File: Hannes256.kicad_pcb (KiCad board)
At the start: 2 copper layers, 56.3 x 82 mm, 33 parts, among them J1 TED_SOCKET, J2 RAM_SELECTOR, J3 CONN_CS, U1 MOS_7360_TED, U10 41256, U11 41256, U12 41256, U13 41256, U14 41256, U2 GAL20V8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

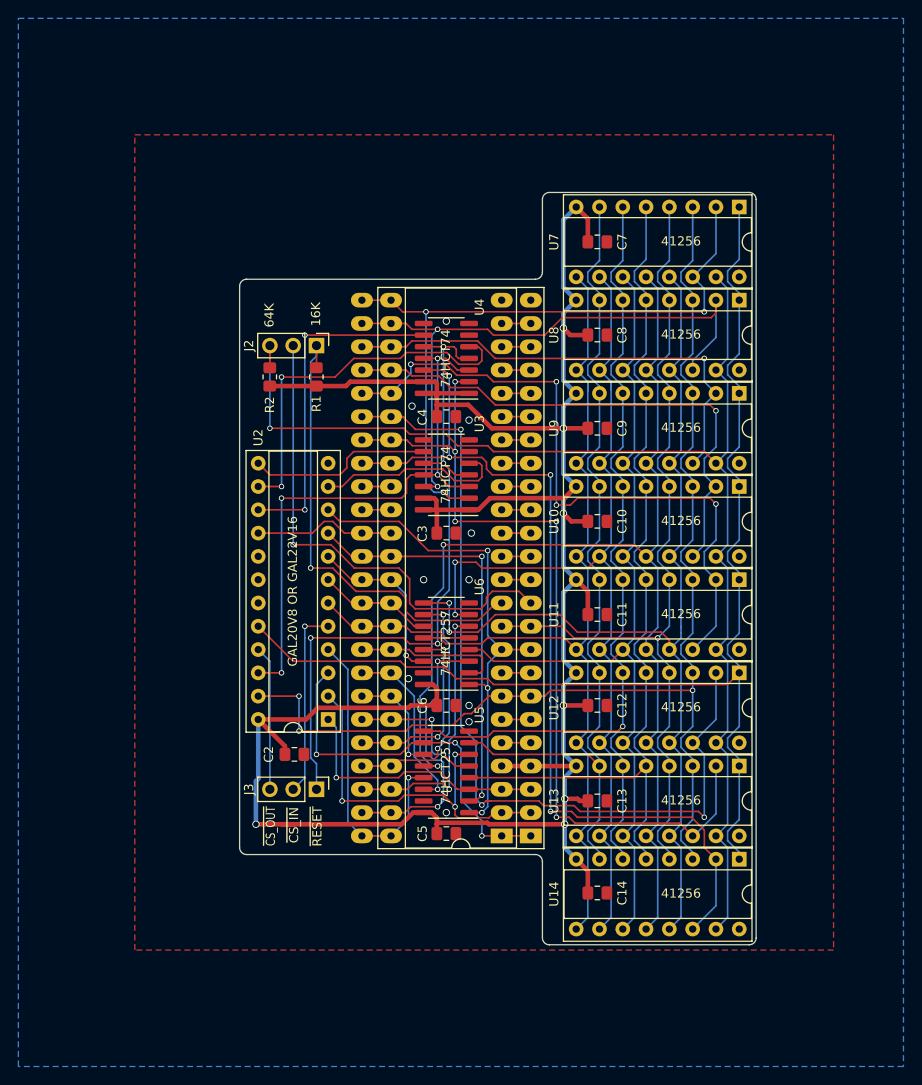
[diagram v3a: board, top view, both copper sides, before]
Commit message: Use a different MOS 6529 replacement circuit, courtesy of TLC
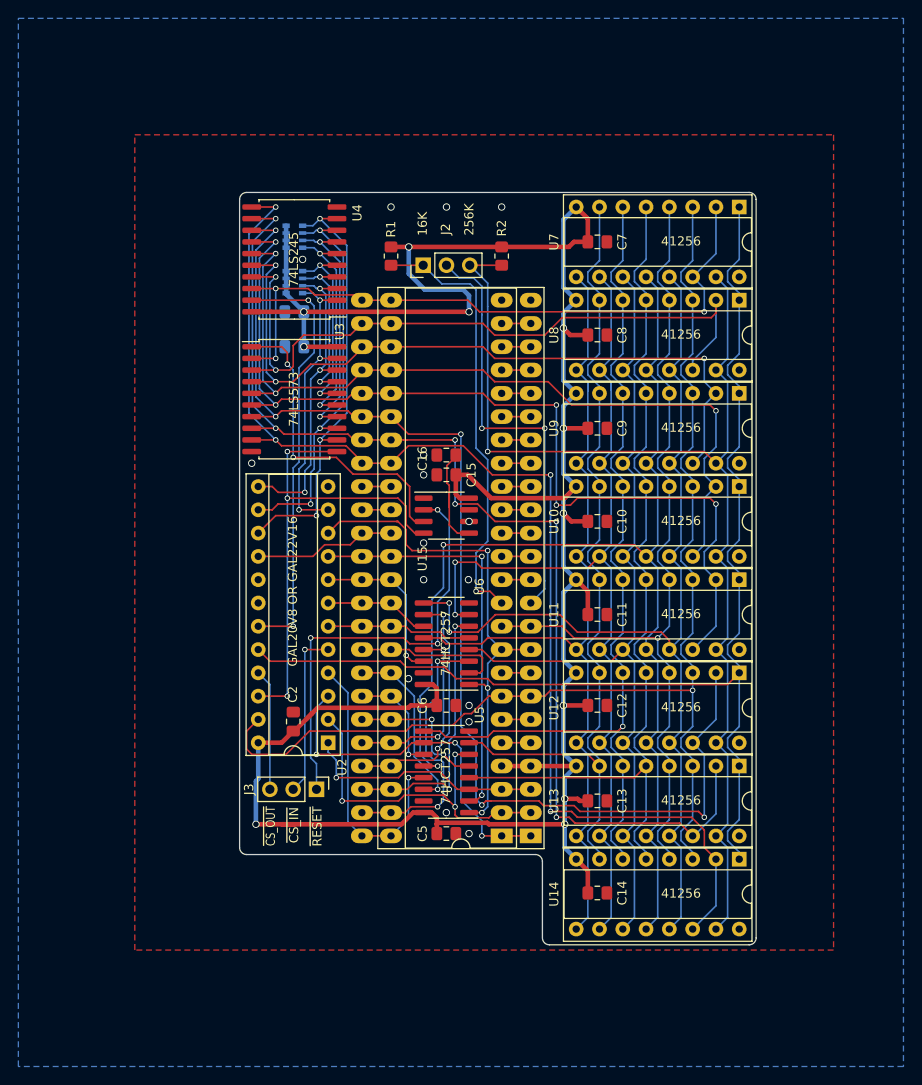
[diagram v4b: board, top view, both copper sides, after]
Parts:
- added C15: 100n, Capacitor_SMD:C_0805_2012Metric_Pad1.18x1.45mm_HandSolder, F.Cu at (126.7, 97.5)
- added C16: 10n, Capacitor_SMD:C_0805_2012Metric_Pad1.18x1.45mm_HandSolder, F.Cu at (126.7, 95.4)
- added RN1: 1k, Resistor_SMD:R_Array_Convex_4x0603, B.Cu at (110.1, 76.5)
- added RN2: 1k, Resistor_SMD:R_Array_Convex_4x0603, B.Cu at (110.1, 71.6)
- added U15: NE555D, Package_SO:SOIC-8_3.9x4.9mm_P1.27mm, F.Cu at (126.7, 102.0)
- C3, C4: moved to B.Cu
- U3: value 74HCT74 -> 74LS573; footprint Package_SO:SOIC-14_3.9x8.7mm_P1.27mm -> Package_SO:SOIC-20W_7.5x12.8mm_P1.27mm
- U4: value 74HCT74 -> 74LS245; footprint Package_SO:SOIC-14_3.9x8.7mm_P1.27mm -> Package_SO:SOIC-20W_7.5x12.8mm_P1.27mm
- moved C3 29.3 mm to (110.1, 79.8), turned to 180 degrees
- moved R2 28.5 mm to (132.7, 73.7), turned to 270 degrees
- moved U4 19.8 mm to (110.1, 74.0)
- moved U3 18.5 mm to (110.1, 89.3), turned to 0 degrees
- moved C4 18.2 mm to (110.1, 83.6), turned to 180 degrees
- moved R1 15.5 mm to (120.7, 73.7), turned to 270 degrees
- moved J2 14.6 mm to (124.2, 74.7), turned to 90 degrees
- moved C2 3.58 mm to (110.0, 124.4), turned to 90 degrees
- moved U2 2.54 mm to (113.8, 126.7)
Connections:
- U2 pad 11: /~RAS~/~CAS~ Generation/p0 -> p0
- U2 pad 13: /~RAS~/~CAS~ Generation/p1 -> p1
- U2 pad 14: /~RAS~/~CAS~ Generation/p6 -> p6
- U2 pad 15: /~RAS~/~CAS~ Generation/p7 -> p7
- U2 pad 19: Net-(U2-Pad19) -> /~RAS~/~CAS~ Generation/~cs_ramrd
- U2 pad 22: /~RAS~/~CAS~ Generation/~cs_ram -> /~RAS~/~CAS~ Generation/~cs_ramwr
- U3 pad 1: +5V -> /~RAS~/~CAS~ Generation/~u3enable
- U3 pad 10: ~RESET -> GND
- U3 pad 11: /~RAS~/~CAS~ Generation/~cs_ram -> /~RAS~/~CAS~ Generation/~cs_ramwr
- U3 pad 12: d1 -> p7
- U3 pad 13: +5V -> p6
- U3 pad 14: +5V -> p5
- U3 pad 3: /~RAS~/~CAS~ Generation/~cs_ram -> d1
- U3 pad 4: ~RESET -> d2
- U3 pad 5: /~RAS~/~CAS~ Generation/p0 -> d3
- U3 pad 6: Net-(U3-Pad6) -> d4
- U3 pad 7: GND -> d5
- U3 pad 8: Net-(U3-Pad8) -> d6
- U3 pad 9: /~RAS~/~CAS~ Generation/p1 -> d7
- U4 pad 10: ~RESET -> GND
- U4 pad 11: /~RAS~/~CAS~ Generation/~cs_ram -> d7
- U4 pad 12: d7 -> d6
- U4 pad 13: +5V -> d5
- U4 pad 14: +5V -> d4
- U4 pad 2: d6 -> p0
- U4 pad 3: /~RAS~/~CAS~ Generation/~cs_ram -> p1
- U4 pad 4: ~RESET -> p2
- U4 pad 5: /~RAS~/~CAS~ Generation/p6 -> p3
- U4 pad 6: Net-(U4-Pad6) -> p4
- U4 pad 7: GND -> p5
- U4 pad 8: Net-(U4-Pad8) -> p6
- U4 pad 9: /~RAS~/~CAS~ Generation/p7 -> p7
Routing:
- net /~RAS~/~CAS~ Generation/~cs_ram: track 62.7 -> 0.00 mm, vias 4 -> 0
- net /~RAS~/~CAS~ Generation/~cs_ramwr: track 0.00 -> 52.9 mm, vias 0 -> 3
- net p7: track 0.00 -> 48.0 mm, vias 0 -> 3
- net /~RAS~/~CAS~ Generation/~cs_ramrd: track 0.00 -> 46.8 mm, vias 0 -> 2
- net p6: track 0.00 -> 44.1 mm, vias 0 -> 3
- net /~RAS~/~CAS~ Generation/p6: track 40.8 -> 0.00 mm, vias 2 -> 0
- net /~RAS~/~CAS~ Generation/p7: track 37.1 -> 0.00 mm, vias 2 -> 0
- net d5: track 96.3 -> 133.3 mm, vias 3 -> 5
- net /~RAS~/~CAS~ Generation/~u3enable: track 0.00 -> 34.9 mm, vias 0 -> 2
- net p1: track 0.00 -> 34.5 mm, vias 0 -> 3
- net p0: track 0.00 -> 32.9 mm, vias 0 -> 3
- net d7: track 100.7 -> 133.0 mm
- net d3: track 58.4 -> 90.6 mm, vias 1 -> 3
- net d6: track 95.8 -> 126.1 mm, vias 5 -> 6
- net d4: track 73.3 -> 103.0 mm, vias 4 -> 5
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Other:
- outline, holes or cut-outs redrawn
- board text added: "256K"
- board text added: "256kB RAM Expansion for the Commodore 16 Based on work by Hannes and Solder/Synergy"
- board text removed: "256kB RAM Expansion for Commodore 16 Based on work by Hannes and Solder/Synergy"
- board text removed: "64K"

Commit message: Update silkscreen
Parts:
- U15: value NE555D -> NE555
- U3: value 74LS573 -> 74HCT573
- U4: value 74LS245 -> 74HCT245
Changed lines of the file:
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@@
       (effects (font (size 1 1) (thickness 0.15)))
     )
-    (fp_text value 74LS573 (at -0.0675 0 90) (layer F.SilkS)
+    (fp_text value 74HCT573 (at -0.0675 0 90) (layer F.SilkS)
       (effects (font (size 1 1) (thickness 0.15)))
     )
@@
       (effects (font (size 1 1) (thickness 0.15)))
     )
-    (fp_text value 74LS245 (at 0.0675 0 90) (layer F.SilkS)
+    (fp_text value 74HCT245 (at 0.0675 0 90) (layer F.SilkS)
       (effects (font (size 1 1) (thickness 0.15)))
     )
@@
       (effects (font (size 1 1) (thickness 0.15)))
     )
-    (fp_text value NE555D (at 0 3.4) (layer F.Fab)
-      (effects (font (size 1 1) (thickness 0.15)))
+    (fp_text value NE555 (at -0.0675 0 90) (layer F.SilkS)
+      (effects (font (size 1 0.9) (thickness 0.15)))
     )
     (fp_line (start 3.7 -2.7) (end -3.7 -2.7) (layer F.CrtYd) (width 0.05))
@@
   (via (at 132.715 68.326) (size 0.8) (drill 0.6) (layers F.Cu B.Cu) (net 18) (status 30))
   (via (at 129.1575 136.652) (size 0.8) (drill 0.6) (layers F.Cu B.Cu) (net 18))
-  (via (at 129.921 110.236) (size 0.6) (drill 0.4) (layers F.Cu B.Cu) (net 33))
   (segment (start 135.89 111.506) (end 137.414 109.982) (width 0.18) (layer B.Cu) (net 19))
   (segment (start 137.414 109.982) (end 137.414 109.093) (width 0.18) (layer B.Cu) (net 19))
@@
   (segment (start 130.556 106.426) (end 130.556 132.461) (width 0.18) (layer B.Cu) (net 32))
   (segment (start 117.475 106.426) (end 113.792 106.426) (width 0.18) (layer F.Cu) (net 32) (status 30))
+  (via (at 129.921 110.236) (size 0.6) (drill 0.4) (layers F.Cu B.Cu) (net 33))
   (segment (start 131.445 110.236) (end 132.715 111.506) (width 0.18) (layer F.Cu) (net 33))
   (segment (start 129.921 110.236) (end 131.445 110.236) (width 0.18) (layer F.Cu) (net 33))

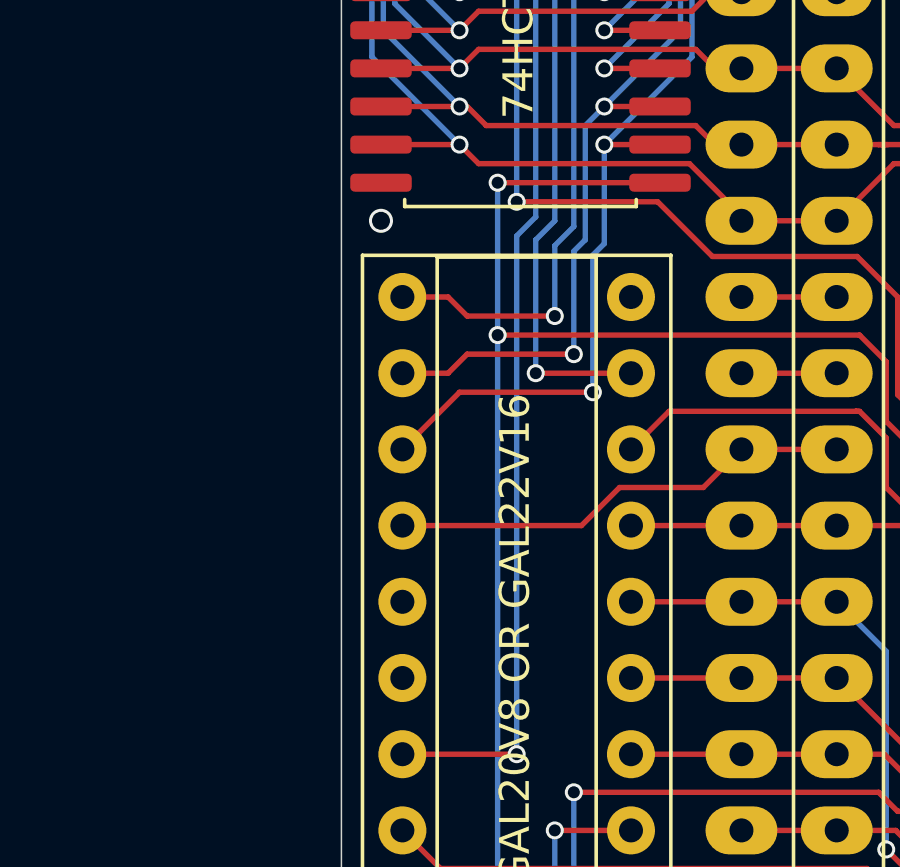
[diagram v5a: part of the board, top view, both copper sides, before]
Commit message: Fix U3 Latch Enable, sigh... GAL equations TBD
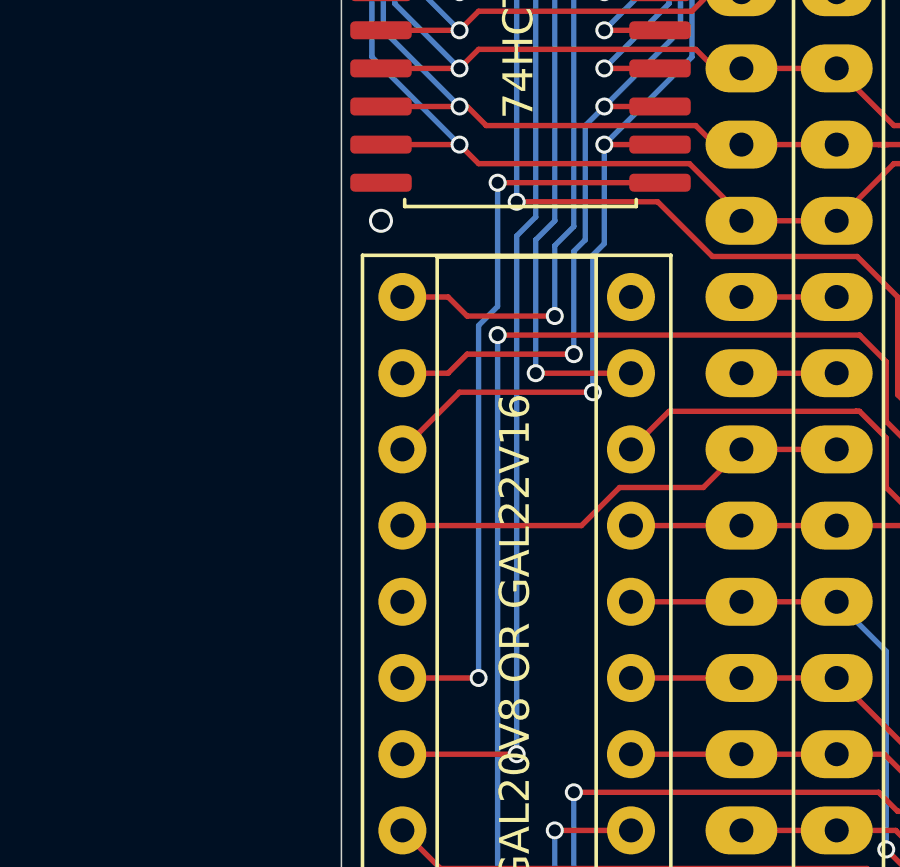
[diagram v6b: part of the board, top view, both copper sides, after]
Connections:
- U2 pad 18: Net-(U2-Pad18) -> /~RAS~/~CAS~ Generation/cs_ramwr
- U3 pad 11: /~RAS~/~CAS~ Generation/~cs_ramwr -> /~RAS~/~CAS~ Generation/cs_ramwr
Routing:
- net /~RAS~/~CAS~ Generation/cs_ramwr: track 0.00 -> 24.7 mm, vias 0 -> 2
- net /~RAS~/~CAS~ Generation/~cs_ramwr: track 52.9 -> 42.4 mm, vias 3 -> 2

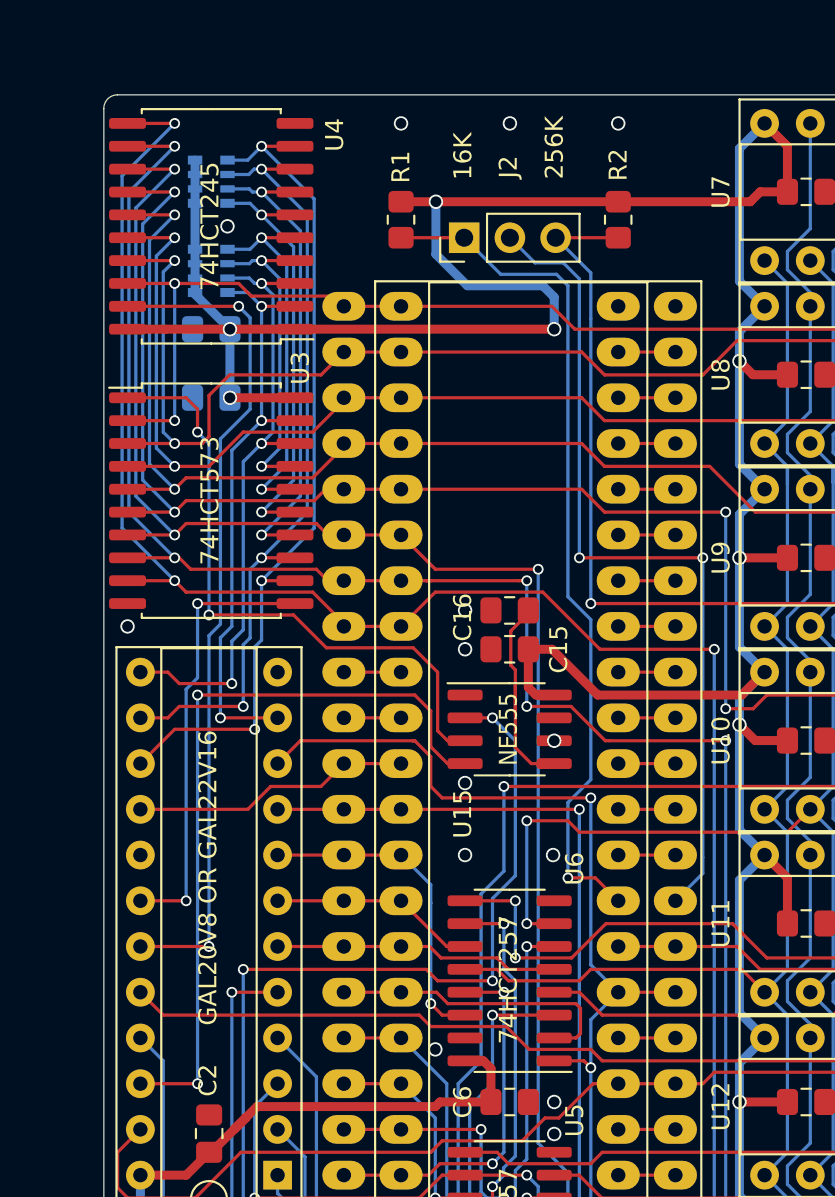
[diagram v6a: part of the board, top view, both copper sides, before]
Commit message: Use narrower footprint for U3/U4 and move everything on the top layer
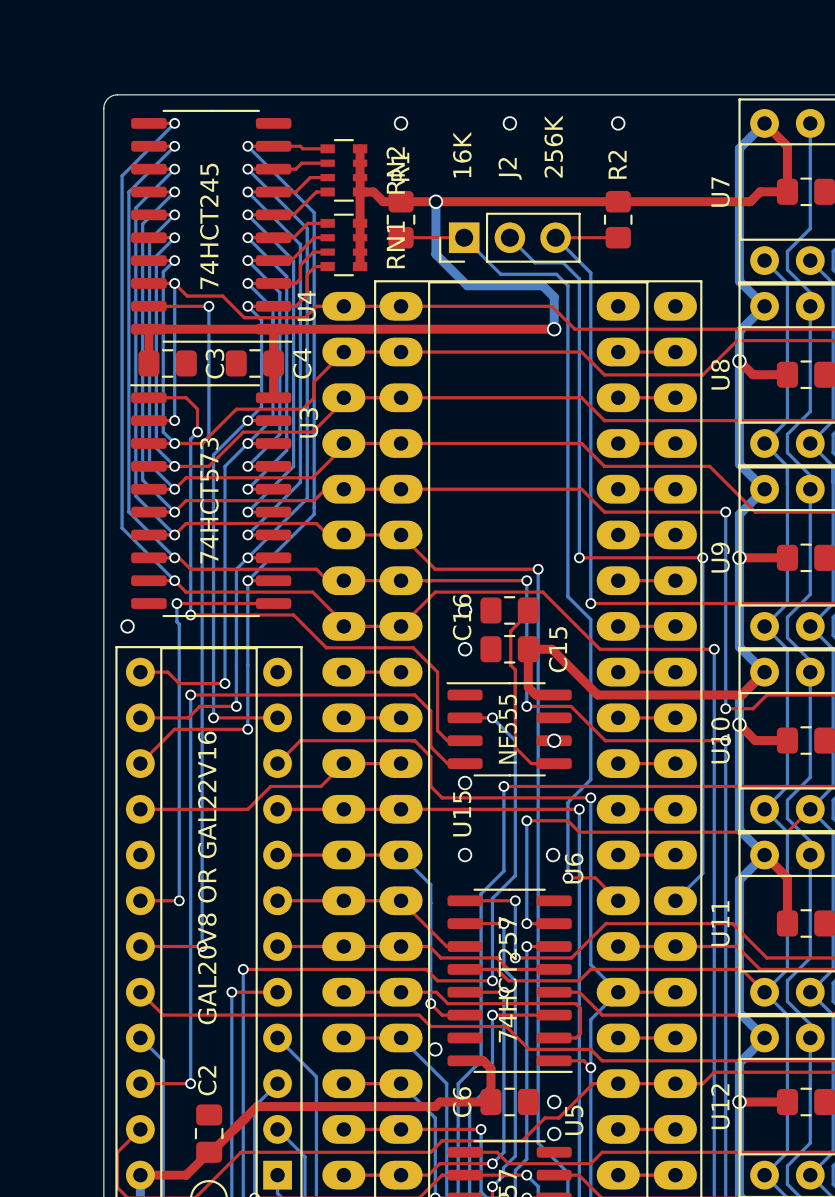
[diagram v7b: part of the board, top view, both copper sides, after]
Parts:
- C3, C4, RN1, RN2: moved to F.Cu
- U3, U4: footprint Package_SO:SOIC-20W_7.5x12.8mm_P1.27mm -> Package_SO:SO-20_5.3x12.6mm_P1.27mm
- moved RN1 7.51 mm to (117.5, 75.1), turned to 0 degrees
- moved RN2 7.39 mm to (117.5, 70.9), turned to 0 degrees
- moved C4 3.08 mm to (112.5, 81.7)
- moved C3 3.08 mm to (107.7, 81.7), turned to 0 degrees
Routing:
- net /~RAS~/~CAS~ Generation/~cs_ramrd: track 46.8 -> 42.5 mm
- net +5V: track 279.7 -> 275.7 mm, vias 11 -> 9
- net d1: track 79.0 -> 75.8 mm
- net p1: track 34.5 -> 37.2 mm
- net d6: track 126.1 -> 123.5 mm
- net p0: track 32.9 -> 35.3 mm
- net d7: track 133.0 -> 130.6 mm
- net d5: track 133.3 -> 130.9 mm
- net d4: track 103.0 -> 100.7 mm
- net d3: track 90.6 -> 88.2 mm
- net d2: track 80.7 -> 78.4 mm
- net d0: track 73.7 -> 71.8 mm
- net p2: track 17.9 -> 19.3 mm
- net p5: track 26.5 -> 27.7 mm
- net p4: track 23.9 -> 25.0 mm
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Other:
- board text added: "V3"
- board text removed: "V2"
